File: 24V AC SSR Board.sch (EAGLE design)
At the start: 41 parts

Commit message: Added new opto-isolators and new custome library
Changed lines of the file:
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@@
 <wire x1="38.1" y1="-30.48" x2="40.64" y2="-30.48" width="0.1524" layer="91"/>
 <pinref part="OK4" gate="-1" pin="A2"/>
-<junction x="40.64" y="-30.48"/>
 <wire x1="40.64" y1="-30.48" x2="43.18" y2="-30.48" width="0.1524" layer="91"/>
 </segment>

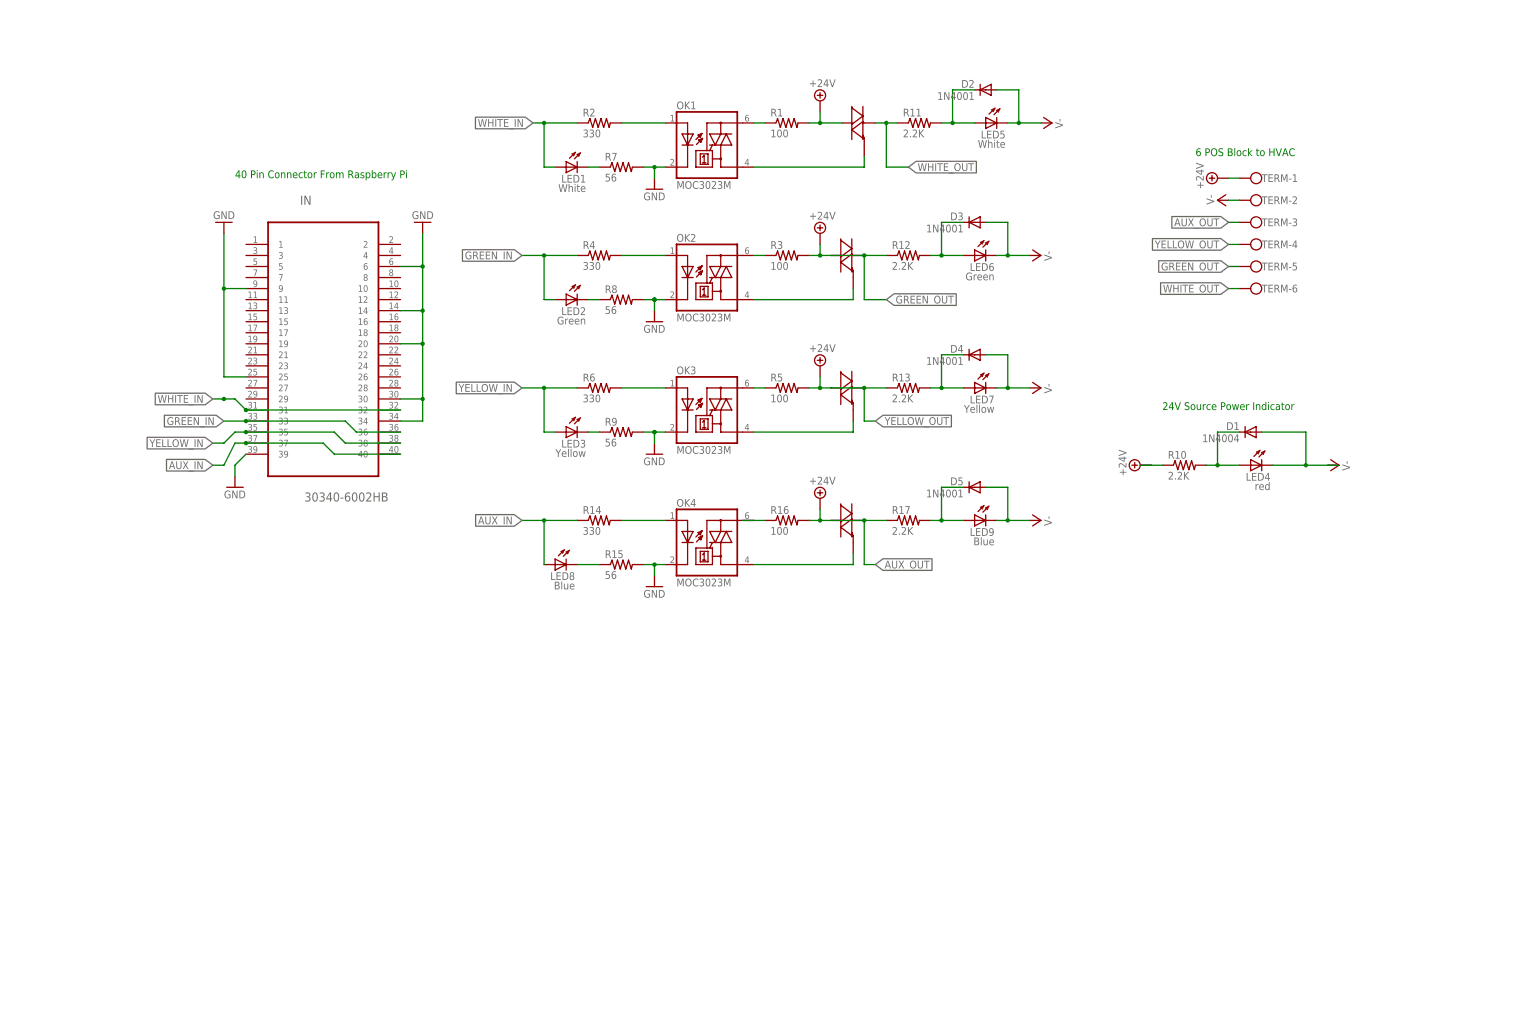
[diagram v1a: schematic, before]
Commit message: Cleaned the board layout
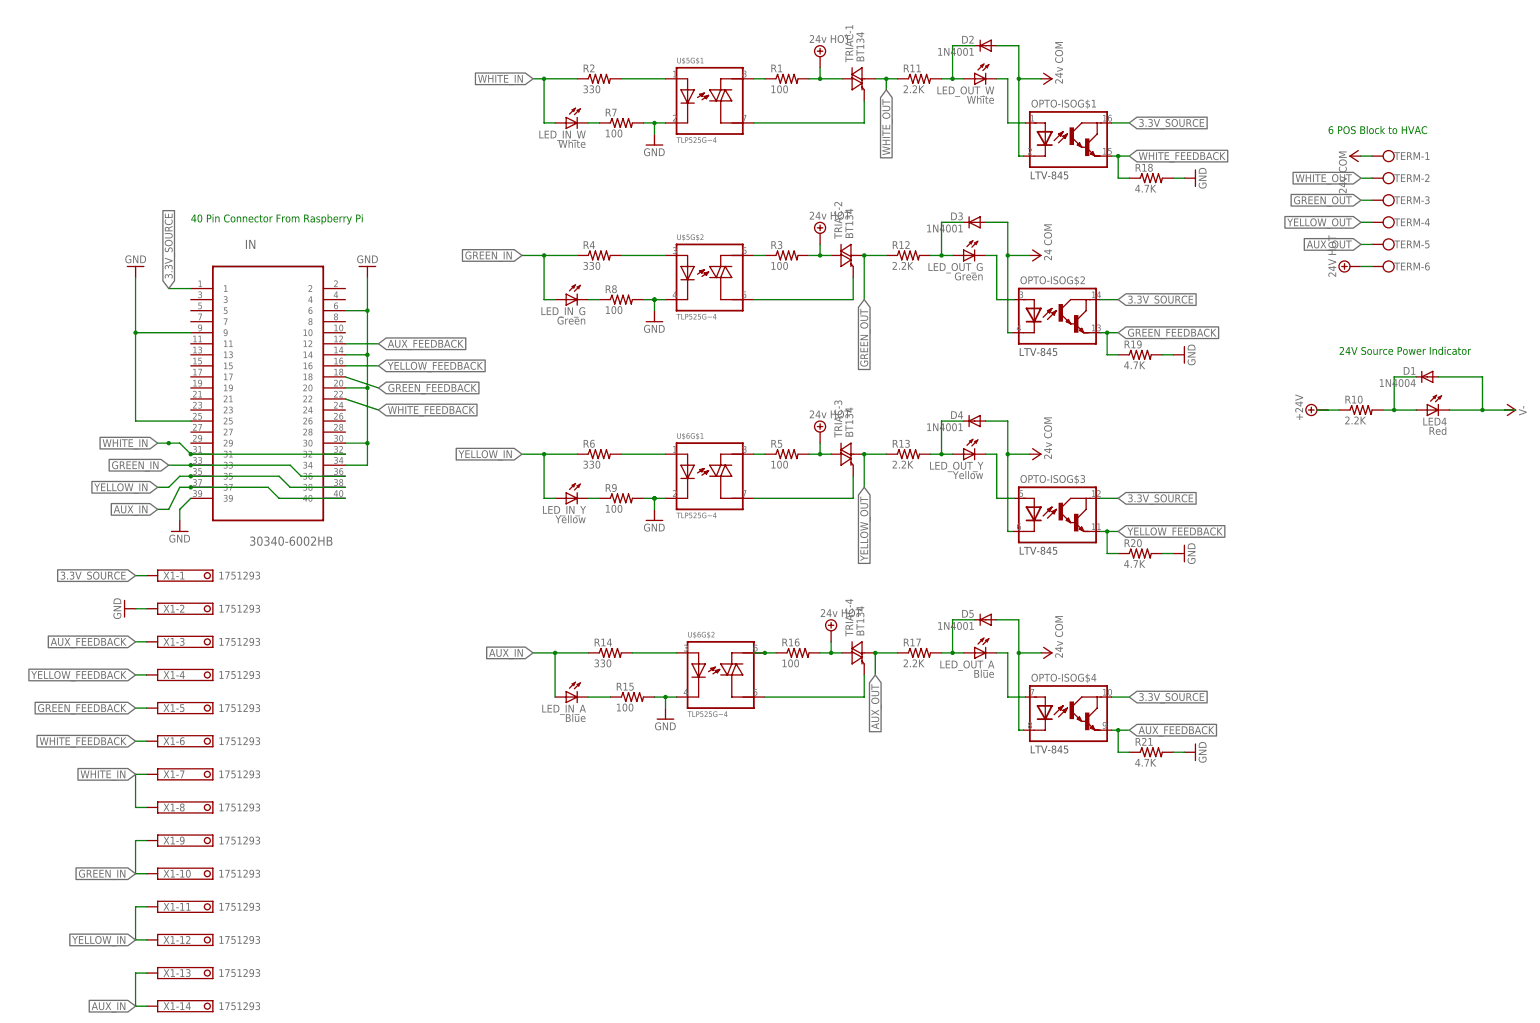
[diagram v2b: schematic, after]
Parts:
- removed LED1, LED5: White, led:LED3MM
- removed LED3, LED7: Yellow, led:LED3MM
- removed LED6: Green, led:LED3MM
- removed LED8, LED9: Blue, led:LED3MM
- removed OK1, OK2, OK3, OK4: MOC3023M, optocoupler:MOC3023M
- removed U$1, U$2, U$3, U$4: BT134, nich:BT134
- added LED_IN_A, LED_OUT_A: Blue, led:LED3MM
- added LED_IN_W, LED_OUT_W: White, led:LED3MM
- added LED_IN_Y, LED_OUT_Y: Yellow, led:LED3MM
- added LED_OUT_G: Green, led:LED3MM
- added OPTO-ISO: LTV-845, myhvac:LTV-845
- added R18, R19, R20, R21: 4.7K, rcl:R-US_0204/7
- added TRIAC-1, TRIAC-2, TRIAC-3, TRIAC-4: BT134, myhvac:BT134
- added U$5, U$6: TLP525G−4, myhvac:TLP525G−4
- added X1: 1751293, myhvac:1751293
- LED4: value red -> Red
- R15, R7, R8, R9: value 56 -> 100
- renumbered LED2 to LED_IN_G
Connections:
- new net 3.3V_SOURCE: IN.1, OPTO-ISOG$1.COLLECTOR, OPTO-ISOG$2.COLLECTOR, OPTO-ISOG$3.COLLECTOR, OPTO-ISOG$4.COLLECTOR, X1-1.K
- new net AUX_FEEDBACK: IN.12, OPTO-ISOG$4.EMITTER, R21.1, X1-3.K
- new net GREEN_FEEDBACK: IN.18, OPTO-ISOG$2.EMITTER, R19.1, X1-5.K
- new net N$11: LED_OUT_G.C, OPTO-ISOG$2.ANNODE
- new net N$13: LED_OUT_Y.C, OPTO-ISOG$3.ANNODE
- new net N$14: LED_OUT_A.C, OPTO-ISOG$4.ANNODE
- new net N$9: LED_OUT_W.C, OPTO-ISOG$1.ANNODE
- new net WHITE_FEEDBACK: IN.22, OPTO-ISOG$1.EMITTER, R18.1, X1-6.K
- new net YELLOW_FEEDBACK: IN.16, OPTO-ISOG$3.EMITTER, R20.1, X1-4.K
- net +24V: now also TERM-6.KL, TRIAC-1.A2, TRIAC-2.A2, TRIAC-3.A2, TRIAC-4.A2; no longer TERM-1.KL, U$1.P$2, U$2.P$2, U$3.P$2, U$4.P$2
- net AUX_IN: now also LED_IN_A.A, X1-13.K, X1-14.K; no longer LED8.A
- net AUX_OUT: now also TERM-5.KL, TRIAC-4.A1; no longer TERM-3.KL, U$4.P$1
- net GND: now also R18.2, R19.2, R20.2, R21.2, U$5G$1.CATHODE, U$5G$2.CATHODE, U$6G$1.CATHODE, U$6G$2.CATHODE, X1-2.K; no longer OK1.C, OK2.C, OK3.C, OK4.C
- net GREEN_IN: now also X1-10.K, X1-9.K
- net GREEN_OUT: now also TERM-3.KL, TRIAC-2.A1; no longer TERM-5.KL, U$2.P$1
- net N$1: now also TRIAC-1.G, U$5G$1.T1; no longer OK1.A1, U$1.P$3
- net N$10: now also U$6G$1.ANNODE; no longer OK3.A
- net N$12: now also U$6G$1.T2; no longer OK3.A2
- net N$17: now also LED_IN_W.C; no longer LED1.C
- net N$2: now also U$5G$1.ANNODE; no longer OK1.A
- net N$20: now also LED_IN_Y.C; no longer LED3.C
- net N$21: now also LED_OUT_W.A; no longer LED5.A
- net N$22: now also LED_OUT_G.A; no longer LED6.A
- net N$23: now also LED_OUT_Y.A; no longer LED7.A
- net N$27: now also U$6G$2.ANNODE; no longer OK4.A
- net N$28: now also LED_IN_A.C; no longer LED8.C
- net N$29: now also U$6G$2.T2; no longer OK4.A2
- net N$3: now also TRIAC-4.G, U$6G$2.T1; no longer OK4.A1, U$4.P$3
- net N$30: now also LED_OUT_A.A; no longer LED9.A
- net N$4: now also U$5G$1.T2; no longer OK1.A2
- net N$5: now also TRIAC-3.G, U$6G$1.T1; no longer OK3.A1, U$3.P$3
- net N$6: now also U$5G$2.ANNODE; no longer OK2.A
- net N$7: now also TRIAC-2.G, U$5G$2.T1; no longer OK2.A1, U$2.P$3
- net N$8: now also U$5G$2.T2; no longer OK2.A2
- net V-: now also OPTO-ISOG$1.CATHODE, OPTO-ISOG$2.CATHODE, OPTO-ISOG$3.CATHODE, OPTO-ISOG$4.CATHODE, TERM-1.KL; no longer LED5.C, LED6.C, LED7.C, LED9.C, TERM-2.KL
- net WHITE_IN: now also LED_IN_W.A, X1-7.K, X1-8.K; no longer LED1.A
- net WHITE_OUT: now also TERM-2.KL, TRIAC-1.A1; no longer TERM-6.KL, U$1.P$1
- net YELLOW_IN: now also LED_IN_Y.A, X1-11.K, X1-12.K; no longer LED3.A
- net YELLOW_OUT: now also TRIAC-3.A1; no longer U$3.P$1
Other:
- moved on the sheet: D1, D2, D4, D5, IN, LED4, R1, R10, R11, R13, R14, R15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

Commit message: Added Photon Board schematics and board
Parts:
- added T3-: 6-POS-SCREW-TERM-PT-3.5MM, myhvac:6-POS-SCREW-TERM-PT-3.5MM
- R18, R19, R20, R21: value 4.7K -> 100K
- TERM: value (none) -> OUT BLOCK
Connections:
- net 3.3V_SOURCE renamed 3.3V_SRC1
- new net 3.3V-SRC2: IN.17, T3-G$1.K
- new net 5V-SRC1: IN.2, T3-G$2.K
- new net GCLK: IN.7, T3-G$6.K
- new net SCL: IN.5, T3-G$5.K
- new net SDA: IN.3, T3-G$4.K
- net GND: now also T3-G$3.K
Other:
- note added: "14 POS input block"
- moved on the sheet: D1, IN, LED4, R10, TERM-1, TERM-2, TERM-3, TERM-4, TERM-5, TERM-6, X1-1, X1-10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
